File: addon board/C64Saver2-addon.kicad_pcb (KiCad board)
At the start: 2 copper layers, 43.9 x 29 mm, 39 parts, among them CON1 AVR-ISP-6, J1 Conn_01x08_Female, J2 Conn_01x08_Female, J3 OLED_128x32_Conn_01x04_Male, J4 Conn_01x04_Female, SW1 SW_Push, U1 INA219xIDR-SOIC, U2 ISO1541D, U3 ATTINY85-20SU, U4 TLP291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

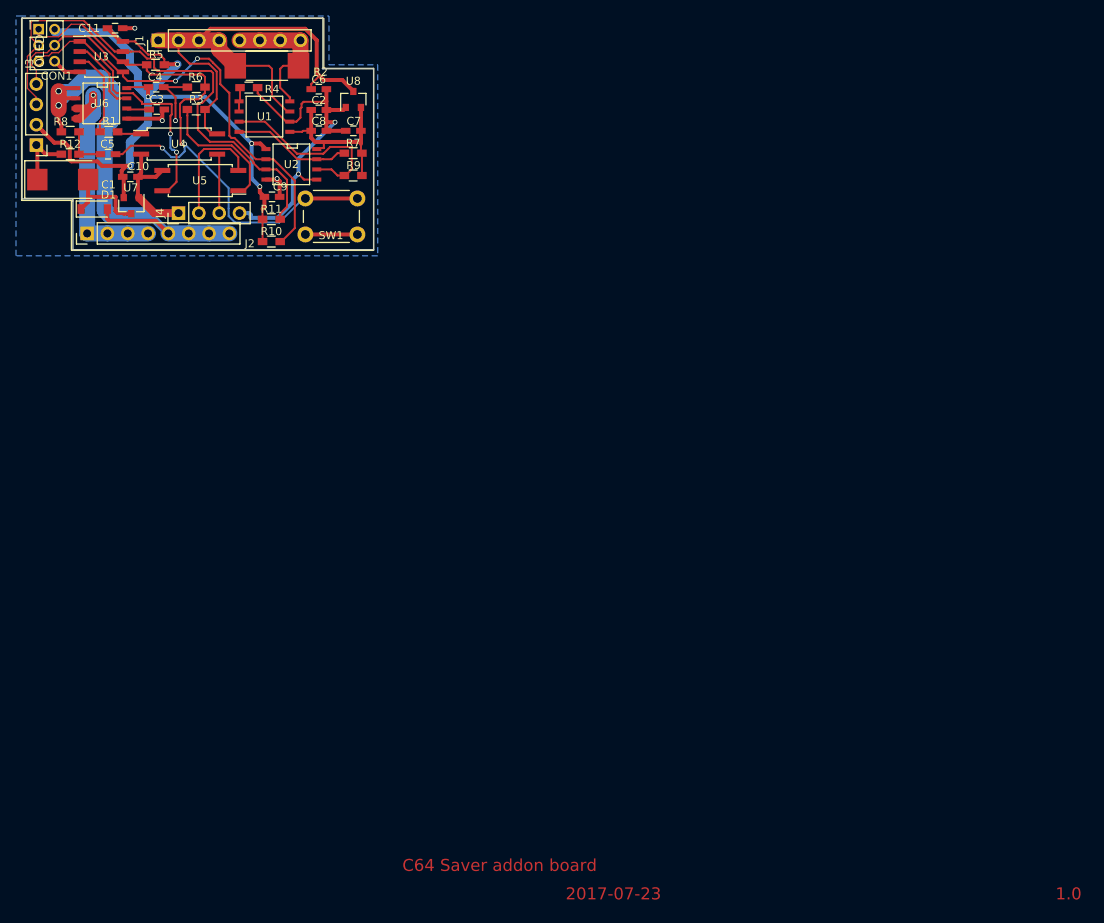
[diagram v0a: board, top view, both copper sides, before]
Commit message: Change: ATtiny footprint, ADC used with reset input
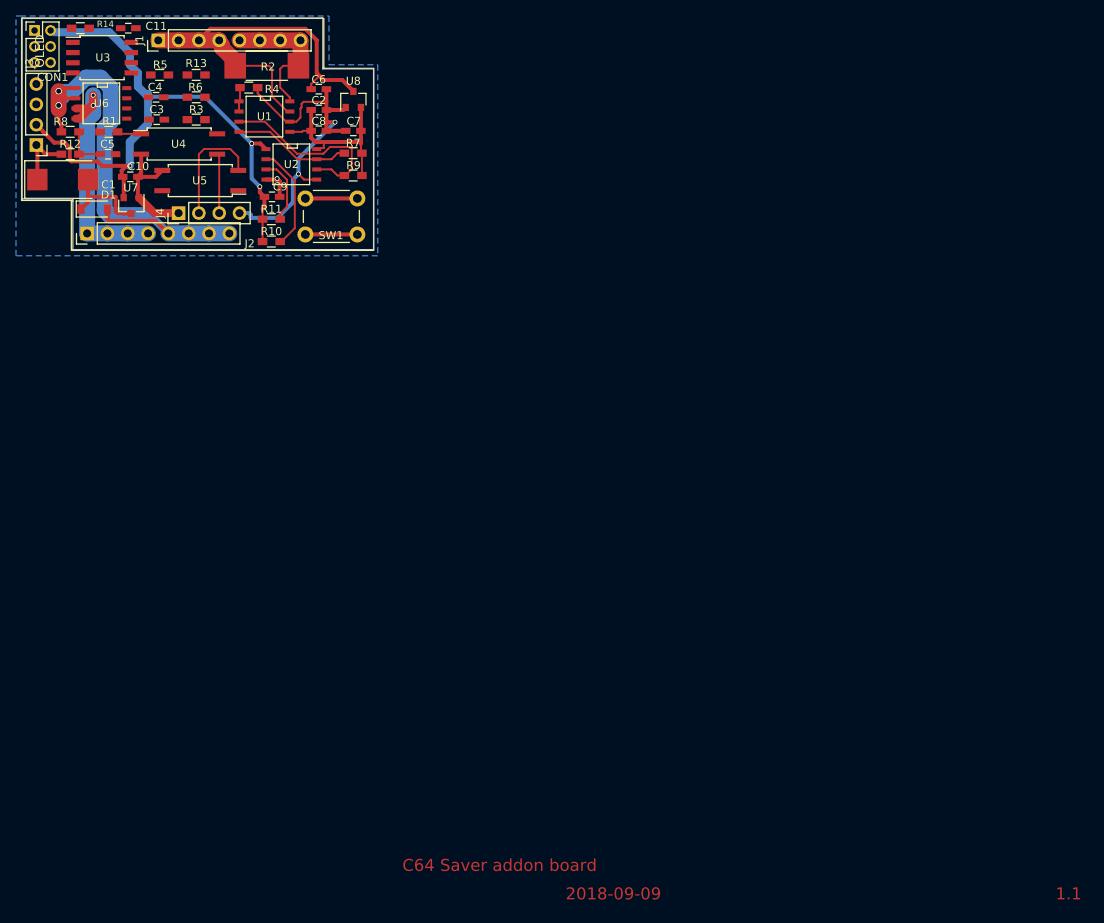
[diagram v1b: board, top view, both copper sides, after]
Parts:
- added R13: 10k, Resistors_SMD:R_0603_HandSoldering, F.Cu at (162.2, 90.7)
- added R14: 1k, Resistors_SMD:R_0603_HandSoldering, F.Cu at (147.7, 84.8)
- U3: footprint Housings_SOIC:SOIC-8_3.9x4.9mm_Pitch1.27mm -> Housings_SOIC:SOIJ-8_5.3x5.3mm_Pitch1.27mm
- moved C11 1.65 mm to (153.7, 84.8)
- moved R5 1.37 mm to (157.7, 90.7)
- moved C3 1.27 mm to (157.3, 96.3)
- moved R3 1.27 mm to (162.2, 96.3)
- moved C4 1.27 mm to (157.2, 93.5)
- moved R6 1.27 mm to (162.2, 93.5)
- moved CON1 0.53 mm to (142.0, 85.1)
- moved U3 0.16 mm to (150.5, 88.5)
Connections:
- U5 pad 4: /#OVERVOLTAGE -> Net-(R13-Pad2)
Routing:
- net /SENSE_VAC: track 76.3 -> 6.50 mm, vias 2 -> 0
- net /SCL1: track 65.2 -> 8.45 mm
- net /SDA1: track 61.1 -> 13.5 mm, vias 2 -> 0
- net /#OVERVOLTAGE: track 35.4 -> 0.33 mm, vias 2 -> 0
- net +5V: track 97.4 -> 77.1 mm, vias 5 -> 3
- net GND: track 52.9 -> 33.8 mm, vias 4 -> 1
- net Net-(R3-Pad1): track 16.8 -> 0.68 mm
- net VIN-: track 67.4 -> 51.3 mm
- net /HOLD_: track 10.9 -> 0.00 mm
- net /SENSE_ACCUR: track 9.58 -> 0.00 mm
- net /FILTER: track 2.85 -> 0.18 mm
- net Net-(R13-Pad2): track 0.00 -> 0.68 mm
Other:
- board text added: "1.1"
- board text added: "2018-09-09"
- board text added: "C64 Saver Addon Rev 1.1 BWACK 2018"
- board text removed: "1.0"
- board text removed: "2017-07-23"
- board text removed: "C64 Saver Addon Rev 1.0 BWACK 2018"

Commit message: Board rerouted
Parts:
- moved R14 16.2 mm to (162.2, 92.2), turned to 180 degrees
- moved R6 5.64 mm to (157.7, 90.2), turned to 180 degrees
- moved R5 4.60 mm to (162.2, 90.2), turned to 180 degrees
- moved R13 3.56 mm to (162.2, 94.2)
- moved C11 3.18 mm to (150.6, 84.8)
- moved R10 3.06 mm to (171.9, 108.5)
- moved R11 2.30 mm to (171.9, 111.0)
- moved C4 0.08 mm to (157.3, 93.5)
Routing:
- net /SENSE_VAC: track 6.50 -> 99.0 mm
- net GND: track 33.8 -> 108.0 mm, vias 1 -> 4
- net /SCL1: track 8.45 -> 67.9 mm
- net /SDA1: track 13.5 -> 57.1 mm, vias 0 -> 2
- net /#OVERVOLTAGE: track 0.33 -> 30.1 mm, vias 0 -> 1
- net +5V: track 77.1 -> 96.1 mm, vias 3 -> 6
- net Net-(R13-Pad2): track 0.68 -> 16.0 mm
- net Net-(R3-Pad1): track 0.68 -> 15.2 mm
- net VIN-: track 51.3 -> 62.3 mm, vias 0 -> 2
- net /HOLD_: track 0.00 -> 10.3 mm
- net /SENSE_ACCUR: track 0.00 -> 9.33 mm
- net /FILTER: track 0.18 -> 3.56 mm

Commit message: Addon board ready for new release #9
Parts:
- U7, U8: value MCP1700-5002E_SOT23 -> MCP1703
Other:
- board text added: "2018-09-23"
- board text removed: "2018-09-09"
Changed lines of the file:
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@@
   )
   (setup
-    (last_trace_width 0.5)
+    (last_trace_width 0.25)
     (user_trace_width 0.127)
     (user_trace_width 0.5)
@@
     (pad 4 thru_hole oval (at 0 7.62 180) (size 1.7 1.7) (drill 1) (layers *.Cu *.Mask)
       (net 13 /SDA1))
-    (model ${KISYS3DMOD}/Pin_Headers.3dshapes/Pin_Header_Straight_1x04_Pitch2.54mm.wrl
-      (at (xyz 0 0 0))
-      (scale (xyz 1 1 1))
-      (rotate (xyz 0 0 0))
+    (model Socket_Strips.3dshapes/Socket_Strip_Straight_1x04_Pitch2.54mm.wrl
+      (at (xyz 0 -0.15 0))
+      (scale (xyz 1 1 1))
+      (rotate (xyz 0 0 90))
     )
   )
@@
       (effects (font (size 1 1) (thickness 0.15)))
     )
-    (fp_text value MCP1700-5002E_SOT23 (at 0 2.5 90) (layer F.Fab)
+    (fp_text value MCP1703 (at 0 2.5 90) (layer F.Fab)
       (effects (font (size 1 1) (thickness 0.15)))
     )
@@
       (effects (font (size 1 1) (thickness 0.15)))
     )
-    (fp_text value MCP1700-5002E_SOT23 (at 0 2.5 270) (layer F.Fab)
+    (fp_text value MCP1703 (at 0 2.5 270) (layer F.Fab)
       (effects (font (size 1 1) (thickness 0.15)))
     )
@@
     (descr "Through hole straight pin header, 1x04, 2.54mm pitch, single row")
     (tags "Through hole pin header THT 1x04 2.54mm single row")
-    (fp_text reference J4 (at 0 -2.33 90) (layer F.SilkS)
+    (fp_text reference J4 (at 0 -2.33 180) (layer F.SilkS)
       (effects (font (size 1 1) (thickness 0.15)))
     )
@@
     (pad 6 thru_hole oval (at 2 4) (size 1.35 1.35) (drill 0.8) (layers *.Cu *.Mask)
       (net 18 GND))
-    (model ${KISYS3DMOD}/Pin_Headers.3dshapes/Pin_Header_Straight_2x03_Pitch2.00mm.wrl
-      (at (xyz 0 0 0))
-      (scale (xyz 1 1 1))
-      (rotate (xyz 0 0 0))
-    )
   )
   (module Capacitors_Tantalum_SMD:CP_Tantalum_Case-X_EIA-7343-43_Reflow (layer F.Cu)
@@
     )
   )
-  (gr_text 2018-09-09 (at 214.376 193.04) (layer F.Cu)
+  (gr_text 2018-09-23 (at 214.376 193.04) (layer F.Cu)
     (effects (font (size 1.5 1.5) (thickness 0.3)))
   )
@@
   (gr_line (start 178.054 83.566) (end 178.054 89.916) (layer Edge.Cuts) (width 0.15))
   (gr_line (start 140.462 83.566) (end 178.054 83.566) (layer Edge.Cuts) (width 0.15))
-  (gr_text OLED (at 142.6845 87.6935 90) (layer F.SilkS)
+  (gr_text OLED (at 144.526 93.726 90) (layer F.SilkS)
     (effects (font (size 1.1 1.1) (thickness 0.275)))
   )
